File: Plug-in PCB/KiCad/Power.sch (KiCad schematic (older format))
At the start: 10 parts, among them J10 Conn_01x01, J11 Conn_01x01, J8 Conn_01x01, J9 Conn_01x01, U2 TPS62402-Q1

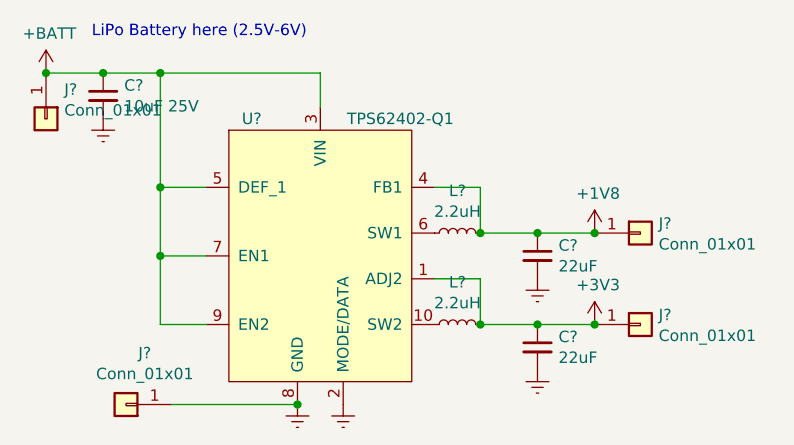
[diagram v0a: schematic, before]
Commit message: Wired Expansion Board Update
1. Begin hardcoding bit-bang communication between wirefree MCU and wired expansion MCU.
++ Can I use the PIO module on the pins to send data in sync while grabbing image from the sensor with parallel capture mode?

2. Wired expansion board schematics and layout modifications
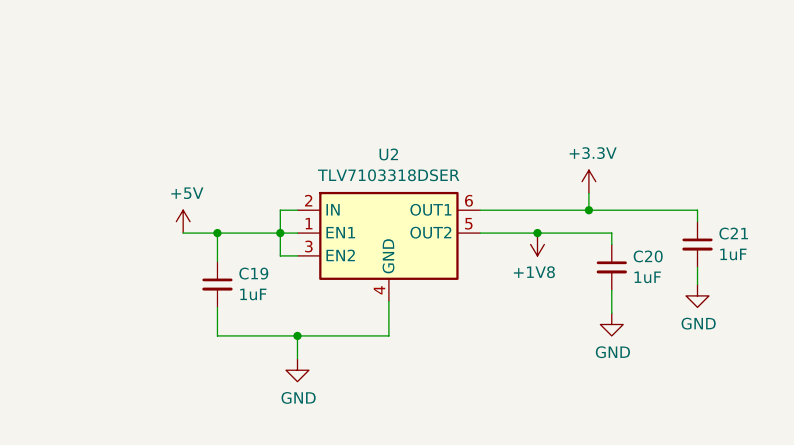
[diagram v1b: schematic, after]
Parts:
- removed C19: GRM21BR61E106MA73L, .Capacitor:C_0805_2012Metric_L, symbol .Capacitor:GRM21BR61E106MA73L
- removed C20, C21: GRM21BR61C226ME44L, .Capacitor:C_0805_2012Metric_L, symbol .Capacitor:GRM21BR61C226ME44L
- removed J10, J11, J8, J9: Conn_01x01, .Connector:Conn_1x1_700_Circular_Pad, symbol .Connector:Conn_01x01
- removed L5, L6: VLS3012HBX-2R2M, .Inductor:VLS3012HBX-2R2M, symbol .Inductor:VLS3012HBX-2R2M
- removed U2: TPS62402-Q1, .Package_SON:SON_10_P50_300X300X100L40X24L, symbol .Regulator_Switching:TPS62402-Q1
- added C19, C20, C21: GRM033R61A105ME15D, .Capacitor:C_0201_0603Metric_L, symbol .Device:C_Small
- added U2: TLV7103318DSER, .Package_SON:SON_6_P50_150X150X80L50X25L, symbol .Regulator_Linear:TLV7103318DSER
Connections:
- net +1V8: now also C20.1, U2.5 (OUT2)
- net +3V3: now also C21.1, U2.6 (OUT1)
- new net +5V: C19.1, U2.1 (EN1), U2.2 (IN), U2.3 (EN2)
- new net GND: C19.2, C20.2, C21.2, U2.4 (GND)
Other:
- note removed: "LiPo Battery here (2.5V-6V)"

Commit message: Wired Expansion Board Updates
1. KiCad: Schematics and layouts completed/Gerber files generated
2. Atmel: Communication protocol from WireFree to WiredExpansion written
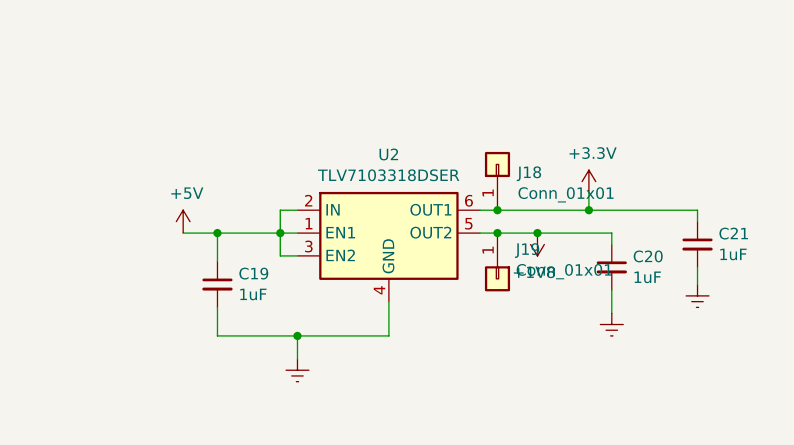
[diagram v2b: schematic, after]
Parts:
- added J18, J19: Conn_01x01, Connector_PinHeader_1.27mm:PinHeader_1x01_P1.27mm_Vertical, symbol .Connector:Conn_01x01
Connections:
- net +1V8: now also J19.1 (Pin_1)
- net +3V3: now also J18.1 (Pin_1)
- net GND renamed Earth
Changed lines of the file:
@@
 Wire Wire Line
 	5850 3500 5850 3350
-$Comp
-L power:GND #PWR0133
-U 1 1 5CC49699
-P 5450 3600
-F 0 "#PWR0133" H 5450 3350 50  0001 C CNN
-F 1 "GND" H 5455 3427 50  0000 C CNN
-F 2 "" H 5450 3600 50  0001 C CNN
-F 3 "" H 5450 3600 50  0001 C CNN
-	1    5450 3600
-	1    0    0    -1
-$EndComp
 Wire Wire Line
 	5450 3600 5450 3500
@@
 $EndComp
 Wire Wire Line
-	6250 3050 6500 3050
+	6250 3050 6325 3050
 Wire Wire Line
 	6500 3050 6825 3050
 Connection ~ 6500 3050
-$Comp
-L power:GND #PWR0136
-U 1 1 5D3F8900
-P 6825 3400
-F 0 "#PWR0136" H 6825 3150 50  0001 C CNN
-F 1 "GND" H 6830 3227 50  0000 C CNN
-F 2 "" H 6825 3400 50  0001 C CNN
-F 3 "" H 6825 3400 50  0001 C CNN
-	1    6825 3400
-	1    0    0    -1
-$EndComp
 Wire Wire Line
-	6250 2950 6725 2950
+	6250 2950 6325 2950
 Wire Wire Line
 	6725 2950 6725 2875
@@
 Wire Wire Line
 	6825 3300 6825 3400
-$Comp
-L power:GND #PWR0137
-U 1 1 5D3F33D9
-P 7200 3275
-F 0 "#PWR0137" H 7200 3025 50  0001 C CNN
-F 1 "GND" H 7205 3102 50  0000 C CNN
-F 2 "" H 7200 3275 50  0001 C CNN
-F 3 "" H 7200 3275 50  0001 C CNN
-	1    7200 3275
-	1    0    0    -1
-$EndComp
 Wire Wire Line
 	7200 3200 7200 3275
@@
 	1    0    0    -1
 $EndComp
+$Comp
+L power:Earth #PWR0120
+U 1 1 5D5F87C6
+P 5450 3600
+F 0 "#PWR0120" H 5450 3350 50  0001 C CNN
+F 1 "Earth" H 5450 3450 50  0001 C CNN
+F 2 "" H 5450 3600 50  0001 C CNN
+F 3 "~" H 5450 3600 50  0001 C CNN
+	1    5450 3600
+	1    0    0    -1
+$EndComp
+$Comp
+L power:Earth #PWR0122
+U 1 1 5D5F897F
+P 6825 3400
+F 0 "#PWR0122" H 6825 3150 50  0001 C CNN
+F 1 "Earth" H 6825 3250 50  0001 C CNN
+F 2 "" H 6825 3400 50  0001 C CNN
+F 3 "~" H 6825 3400 50  0001 C CNN
+	1    6825 3400
+	1    0    0    -1
+$EndComp
+$Comp
+L power:Earth #PWR0125
+U 1 1 5D5F8B3E
+P 7200 3275
+F 0 "#PWR0125" H 7200 3025 50  0001 C CNN
+F 1 "Earth" H 7200 3125 50  0001 C CNN
+F 2 "" H 7200 3275 50  0001 C CNN
+F 3 "~" H 7200 3275 50  0001 C CNN
+	1    7200 3275
+	1    0    0    -1
+$EndComp
+$Comp
+L .Connector:Conn_01x01 J18
+U 1 1 5D3DB94D
+P 6325 2750
+F 0 "J18" V 6289 2662 50  0000 R CNN
+F 1 "Conn_01x01" V 6198 2662 50  0000 R CNN
+F 2 "Connector_PinHeader_1.27mm:PinHeader_1x01_P1.27mm_Vertical" H 6325 2750 50  0001 C CNN
+F 3 "~" H 6325 2750 50  0001 C CNN
+	1    6325 2750
+	0    -1   -1   0
+$EndComp
+Connection ~ 6325 2950
+Wire Wire Line
+	6325 2950 6725 2950
+$Comp
+L .Connector:Conn_01x01 J19
+U 1 1 5D3DC2A8
+P 6325 3250
+F 0 "J19" V 6197 3330 50  0000 L CNN
+F 1 "Conn_01x01" V 6288 3330 50  0000 L CNN
+F 2 "Connector_PinHeader_1.27mm:PinHeader_1x01_P1.27mm_Vertical" H 6325 3250 50  0001 C CNN
+F 3 "~" H 6325 3250 50  0001 C CNN
+	1    6325 3250
+	0    1    1    0
+$EndComp
+Connection ~ 6325 3050
+Wire Wire Line
+	6325 3050 6500 3050
 $EndSCHEMATC

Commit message: Change MCU and Serializer Power to 3.3V
1. MCU VDDIO, SWD, VDDIN, VDDUTMII powered at 3.3V

2. Serializer VDDIO, PDB powered at 3.3V

3. Layout changed (Pins enlarged, Coax_Gnd added, Coax connector moved closer to seralizer)
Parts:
- J18, J19: footprint Connector_PinHeader_1.27mm:PinHeader_1x01_P1.27mm_Vertical -> Connector_PinHeader_2.54mm:PinHeader_1x01_P2.54mm_Vertical
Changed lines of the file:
@@
 F 0 "J18" V 6289 2662 50  0000 R CNN
 F 1 "Conn_01x01" V 6198 2662 50  0000 R CNN
-F 2 "Connector_PinHeader_1.27mm:PinHeader_1x01_P1.27mm_Vertical" H 6325 2750 50  0001 C CNN
+F 2 "Connector_PinHeader_2.54mm:PinHeader_1x01_P2.54mm_Vertical" H 6325 2750 50  0001 C CNN
 F 3 "~" H 6325 2750 50  0001 C CNN
 	1    6325 2750
@@
 F 0 "J19" V 6197 3330 50  0000 L CNN
 F 1 "Conn_01x01" V 6288 3330 50  0000 L CNN
-F 2 "Connector_PinHeader_1.27mm:PinHeader_1x01_P1.27mm_Vertical" H 6325 3250 50  0001 C CNN
+F 2 "Connector_PinHeader_2.54mm:PinHeader_1x01_P2.54mm_Vertical" H 6325 3250 50  0001 C CNN
 F 3 "~" H 6325 3250 50  0001 C CNN
 	1    6325 3250
